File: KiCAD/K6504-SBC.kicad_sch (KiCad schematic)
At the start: 35 parts, among them J5 Barrel_Jack_Switch, SW1 RESET SW, SW2 POWER_SW, U1 R6504P, U3 74LS00, U4 74LS145, U5 R6532, U6 HM62256BLP, U7 27C256, X1 1MHz

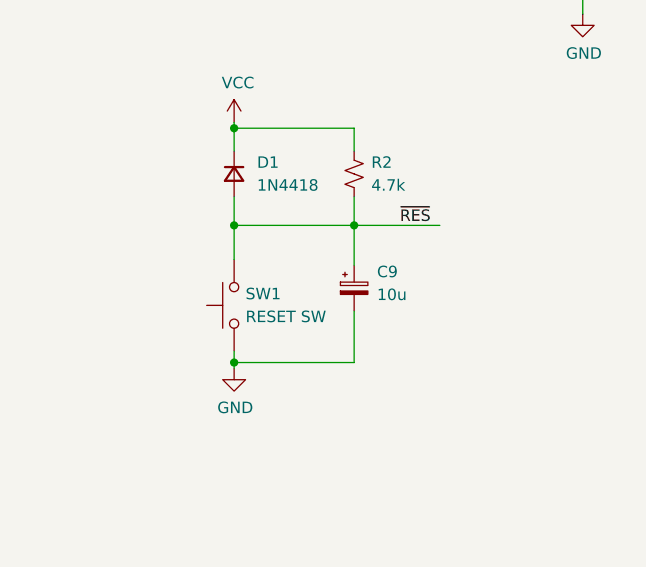
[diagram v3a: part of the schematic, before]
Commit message: 部品との関連付け追加
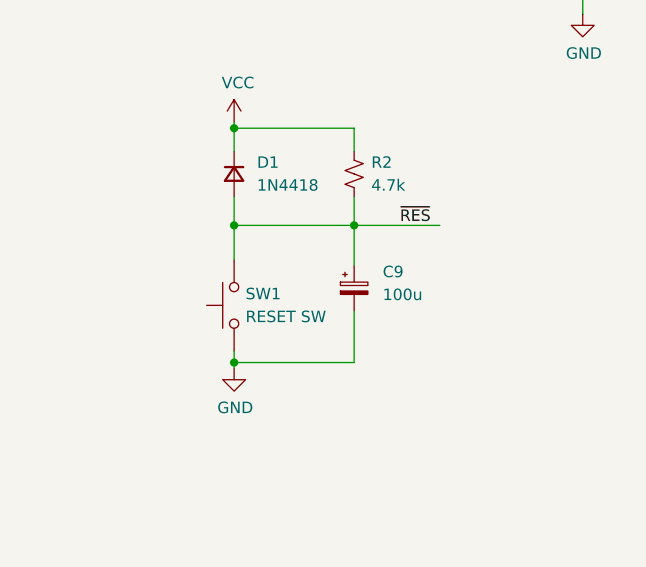
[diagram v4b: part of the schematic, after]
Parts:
- C10: footprint (none) -> Capacitor_THT:CP_Radial_D5.0mm_P2.50mm
- C9: value 10u -> 100u; footprint (none) -> Capacitor_THT:CP_Radial_D8.0mm_P2.50mm
- D1: footprint (none) -> Diode_THT:D_DO-34_SOD68_P10.16mm_Horizontal
- D2: footprint (none) -> LED_THT:LED_D3.0mm
- J5: footprint (none) -> Connector_BarrelJack:BarrelJack_Horizontal
- R2, R3: footprint (none) -> Resistor_THT:R_Axial_DIN0207_L6.3mm_D2.5mm_P10.16mm_Horizontal
- SW1: footprint (none) -> Button_Switch_THT:SW_PUSH_6mm_H4.3mm
- SW2: footprint (none) -> Connector_PinHeader_2.54mm:PinHeader_1x03_P2.54mm_Vertical
- U1, U6, U7: footprint Package_DIP:DIP-28_W15.24mm -> Package_DIP:DIP-28_W15.24mm_Socket
- U3: footprint (none) -> Package_DIP:DIP-14_W7.62mm_Socket
- U4: footprint (none) -> Package_DIP:DIP-16_W7.62mm_Socket
- U5: footprint Package_DIP:DIP-40_W15.24mm -> Package_DIP:DIP-40_W15.24mm_Socket
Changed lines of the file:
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@@
       (effects (font (size 1.27 1.27)))
     )
-    (property "Footprint" "" (at 285.115 56.896 0)
+    (property "Footprint" "Connector_BarrelJack:BarrelJack_Horizontal" (at 285.115 56.896 0)
       (effects (font (size 1.27 1.27)) hide)
     )
@@
       (effects (font (size 1.27 1.27)) (justify left))
     )
-    (property "Footprint" "Package_DIP:DIP-28_W15.24mm" (at 273.685 184.15 0)
+    (property "Footprint" "Package_DIP:DIP-28_W15.24mm_Socket" (at 273.685 184.15 0)
       (effects (font (size 1.27 1.27)) hide)
     )
@@
   (symbol (lib_id "Device:C_Polarized_Small") (at 309.245 99.06 0) (unit 1)
     (in_bom yes) (on_board yes) (dnp no) (fields_autoplaced)
-    (property "Reference" "C9" (at 311.785 97.2439 0)
-      (effects (font (size 1.27 1.27)) (justify left))
-    )
-    (property "Value" "10u" (at 311.785 99.7839 0)
-      (effects (font (size 1.27 1.27)) (justify left))
-    )
-    (property "Footprint" "" (at 309.245 99.06 0)
+    (property "Reference" "C9" (at 312.42 97.2439 0)
+      (effects (font (size 1.27 1.27)) (justify left))
+    )
+    (property "Value" "100u" (at 312.42 99.7839 0)
+      (effects (font (size 1.27 1.27)) (justify left))
+    )
+    (property "Footprint" "Capacitor_THT:CP_Radial_D8.0mm_P2.50mm" (at 309.245 99.06 0)
       (effects (font (size 1.27 1.27)) hide)
     )
@@
       (effects (font (size 1.27 1.27)) (justify left))
     )
-    (property "Footprint" "" (at 227.965 254 0)
+    (property "Footprint" "Package_DIP:DIP-14_W7.62mm_Socket" (at 227.965 254 0)
       (effects (font (size 1.27 1.27)) hide)
     )
@@
       (effects (font (size 1.27 1.27)) (justify left))
     )
-    (property "Footprint" "" (at 313.055 53.975 0)
+    (property "Footprint" "Capacitor_THT:CP_Radial_D5.0mm_P2.50mm" (at 313.055 53.975 0)
       (effects (font (size 1.27 1.27)) hide)
     )
@@
       (effects (font (size 1.27 1.27)) (justify left))
     )
-    (property "Footprint" "Package_DIP:DIP-28_W15.24mm" (at 224.79 180.34 0)
+    (property "Footprint" "Package_DIP:DIP-28_W15.24mm_Socket" (at 224.79 180.34 0)
       (effects (font (size 1.27 1.27)) hide)
     )
@@
       (effects (font (size 1.27 1.27)) (justify left))
     )
-    (property "Footprint" "" (at 324.485 50.8 0)
+    (property "Footprint" "Resistor_THT:R_Axial_DIN0207_L6.3mm_D2.5mm_P10.16mm_Horizontal" (at 324.485 50.8 0)
       (effects (font (size 1.27 1.27)) hide)
     )
@@
       (effects (font (size 1.27 1.27)))
     )
-    (property "Footprint" "" (at 302.895 46.355 0)
+    (property "Footprint" "Connector_PinHeader_2.54mm:PinHeader_1x03_P2.54mm_Vertical" (at 302.895 46.355 0)
       (effects (font (size 1.27 1.27)) hide)
     )
@@
       (effects (font (size 1.27 1.27)) (justify left))
     )
-    (property "Footprint" "Package_DIP:DIP-40_W15.24mm" (at 158.75 220.98 0)
+    (property "Footprint" "Package_DIP:DIP-40_W15.24mm_Socket" (at 158.75 220.98 0)
       (effects (font (size 1.27 1.27)) (justify left) hide)
     )
@@
       (effects (font (size 1.27 1.27)))
     )
-    (property "Footprint" "" (at 120.015 199.39 0)
+    (property "Footprint" "Package_DIP:DIP-14_W7.62mm_Socket" (at 120.015 199.39 0)
       (effects (font (size 1.27 1.27)) hide)
     )
@@
       (effects (font (size 1.27 1.27)) (justify left))
     )
-    (property "Footprint" "" (at 295.91 86.36 90)
+    (property "Footprint" "Diode_THT:D_DO-34_SOD68_P10.16mm_Horizontal" (at 295.91 86.36 90)
       (effects (font (size 1.27 1.27)) hide)
     )
@@
       (effects (font (size 1.27 1.27)))
     )
-    (property "Footprint" "" (at 229.87 104.775 0)
+    (property "Footprint" "Package_DIP:DIP-14_W7.62mm_Socket" (at 229.87 104.775 0)
       (effects (font (size 1.27 1.27)) hide)
     )
@@
       (effects (font (size 1.27 1.27)) (justify left))
     )
-    (property "Footprint" "" (at 153.035 48.895 0)
+    (property "Footprint" "Package_DIP:DIP-16_W7.62mm_Socket" (at 153.035 48.895 0)
       (effects (font (size 1.27 1.27)) hide)
     )
@@
       (effects (font (size 1.27 1.27)))
     )
-    (property "Footprint" "" (at 189.865 102.235 0)
+    (property "Footprint" "Package_DIP:DIP-14_W7.62mm_Socket" (at 189.865 102.235 0)
       (effects (font (size 1.27 1.27)) hide)
     )
@@
       (effects (font (size 1.27 1.27)))
     )
-    (property "Footprint" "" (at 229.235 122.555 0)
+    (property "Footprint" "Package_DIP:DIP-14_W7.62mm_Socket" (at 229.235 122.555 0)
       (effects (font (size 1.27 1.27)) hide)
     )
@@
       (effects (font (size 1.27 1.27)) (justify left))
     )
-    (property "Footprint" "" (at 309.245 86.36 0)
+    (property "Footprint" "Resistor_THT:R_Axial_DIN0207_L6.3mm_D2.5mm_P10.16mm_Horizontal" (at 309.245 86.36 0)
       (effects (font (size 1.27 1.27)) hide)
     )
@@
       (effects (font (size 1.27 1.27)) (justify right))
     )
-    (property "Footprint" "" (at 290.83 100.965 0)
+    (property "Footprint" "Button_Switch_THT:SW_PUSH_6mm_H4.3mm" (at 290.83 100.965 0)
       (effects (font (size 1.27 1.27)) hide)
     )
@@
       (effects (font (size 1.27 1.27)) (justify left))
     )
-    (property "Footprint" "Package_DIP:DIP-28_W15.24mm" (at 61.595 193.04 0)
+    (property "Footprint" "Package_DIP:DIP-28_W15.24mm_Socket" (at 61.595 193.04 0)
       (effects (font (size 1.27 1.27)) hide)
     )
@@
       (effects (font (size 1.27 1.27)) (justify right))
     )
-    (property "Footprint" "" (at 324.485 58.42 90)
-      (effects (font (size 1.27 1.27)) hide)
-    )
+    (property "Footprint" "LED_THT:LED_D3.0mm" (at 324.485 58.42 90)
+      (effects (font (size 1.27 1.27)) hide)
+    )

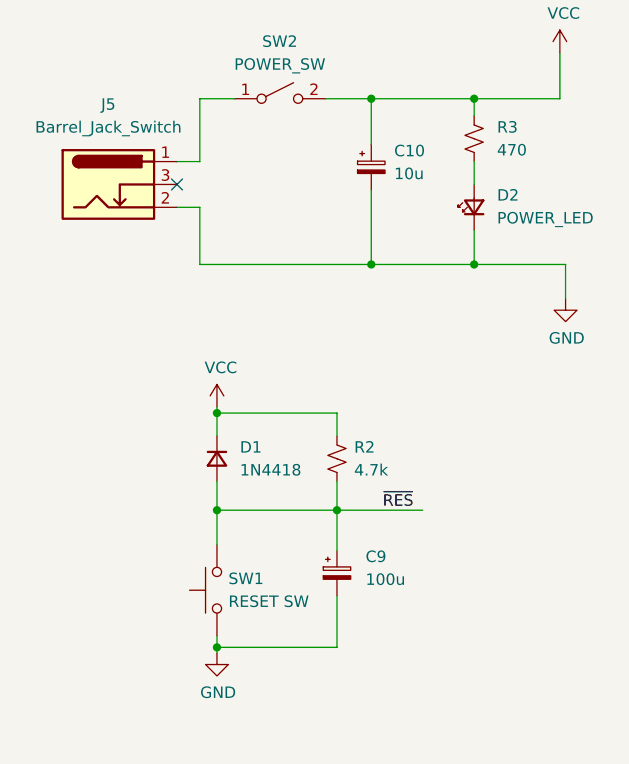
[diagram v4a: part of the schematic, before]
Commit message: コンデンサ定数修正、回路図イメージ更新
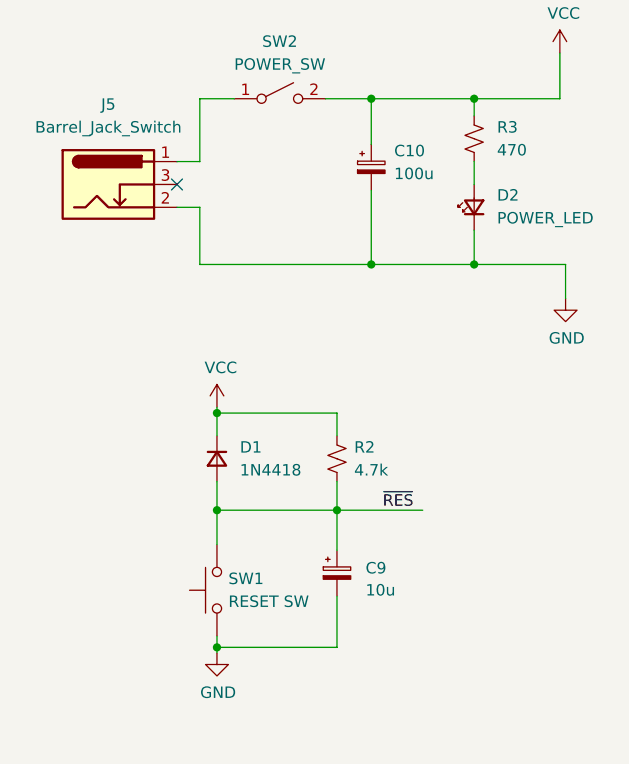
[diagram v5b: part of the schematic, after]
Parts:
- C10: value 10u -> 100u; footprint Capacitor_THT:CP_Radial_D5.0mm_P2.50mm -> Capacitor_THT:CP_Radial_D8.0mm_P2.50mm
- C9: value 100u -> 10u; footprint Capacitor_THT:CP_Radial_D8.0mm_P2.50mm -> Capacitor_THT:CP_Radial_D5.0mm_P2.50mm
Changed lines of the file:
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@@
   )
   (symbol (lib_id "Device:C_Polarized_Small") (at 309.245 99.06 0) (unit 1)
-    (in_bom yes) (on_board yes) (dnp no) (fields_autoplaced)
-    (property "Reference" "C9" (at 312.42 97.2439 0)
-      (effects (font (size 1.27 1.27)) (justify left))
-    )
-    (property "Value" "100u" (at 312.42 99.7839 0)
-      (effects (font (size 1.27 1.27)) (justify left))
-    )
-    (property "Footprint" "Capacitor_THT:CP_Radial_D8.0mm_P2.50mm" (at 309.245 99.06 0)
+    (in_bom yes) (on_board yes) (dnp no)
+    (property "Reference" "C9" (at 312.42 98.5139 0)
+      (effects (font (size 1.27 1.27)) (justify left))
+    )
+    (property "Value" "10u" (at 312.42 100.965 0)
+      (effects (font (size 1.27 1.27)) (justify left))
+    )
+    (property "Footprint" "Capacitor_THT:CP_Radial_D5.0mm_P2.50mm" (at 309.245 99.06 0)
       (effects (font (size 1.27 1.27)) hide)
     )
@@
       (effects (font (size 1.27 1.27)) (justify left))
     )
-    (property "Value" "10u" (at 315.595 54.6989 0)
-      (effects (font (size 1.27 1.27)) (justify left))
-    )
-    (property "Footprint" "Capacitor_THT:CP_Radial_D5.0mm_P2.50mm" (at 313.055 53.975 0)
-      (effects (font (size 1.27 1.27)) hide)
-    )
+    (property "Value" "100u" (at 315.595 54.6989 0)
+      (effects (font (size 1.27 1.27)) (justify left))
+    )
+    (property "Footprint" "Capacitor_THT:CP_Radial_D8.0mm_P2.50mm" (at 313.055 53.975 0)
+      (effects (font (size 1.27 1.27)) hide)
+    )

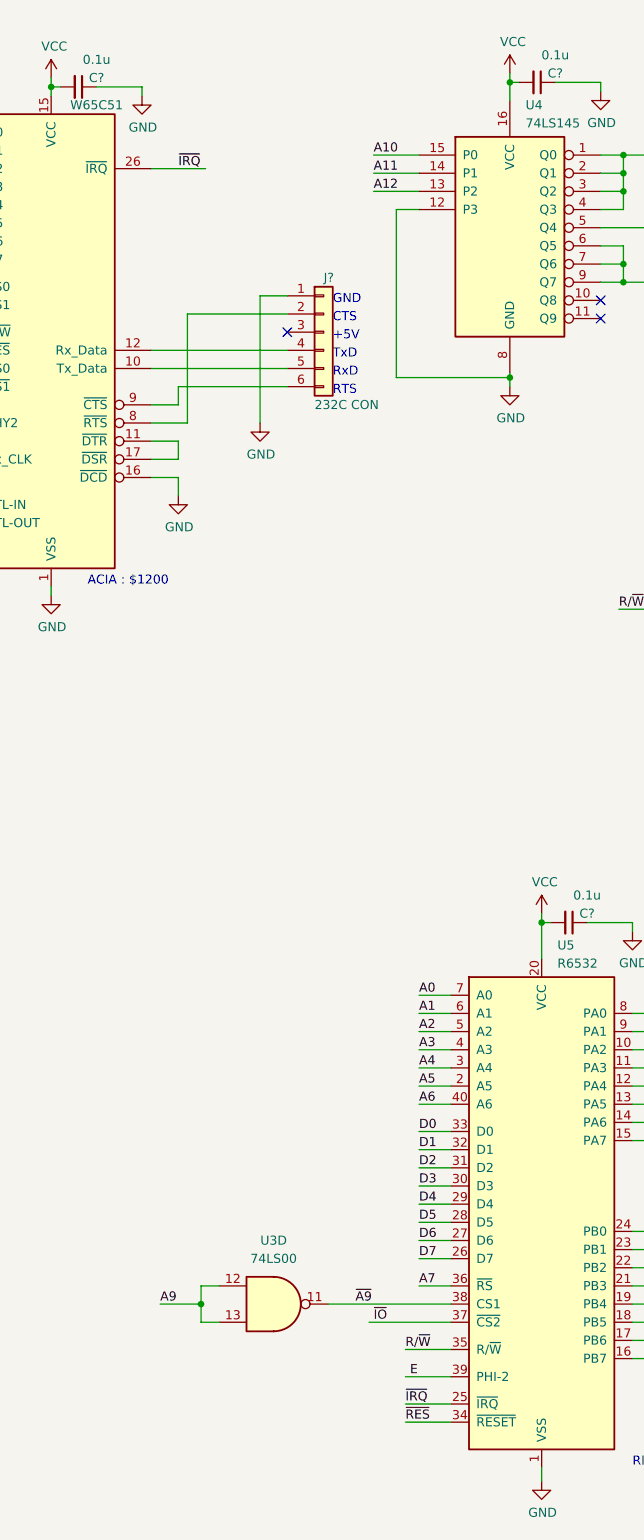
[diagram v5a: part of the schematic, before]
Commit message: 基板サイズ見直し、ガーバーデータ再出力
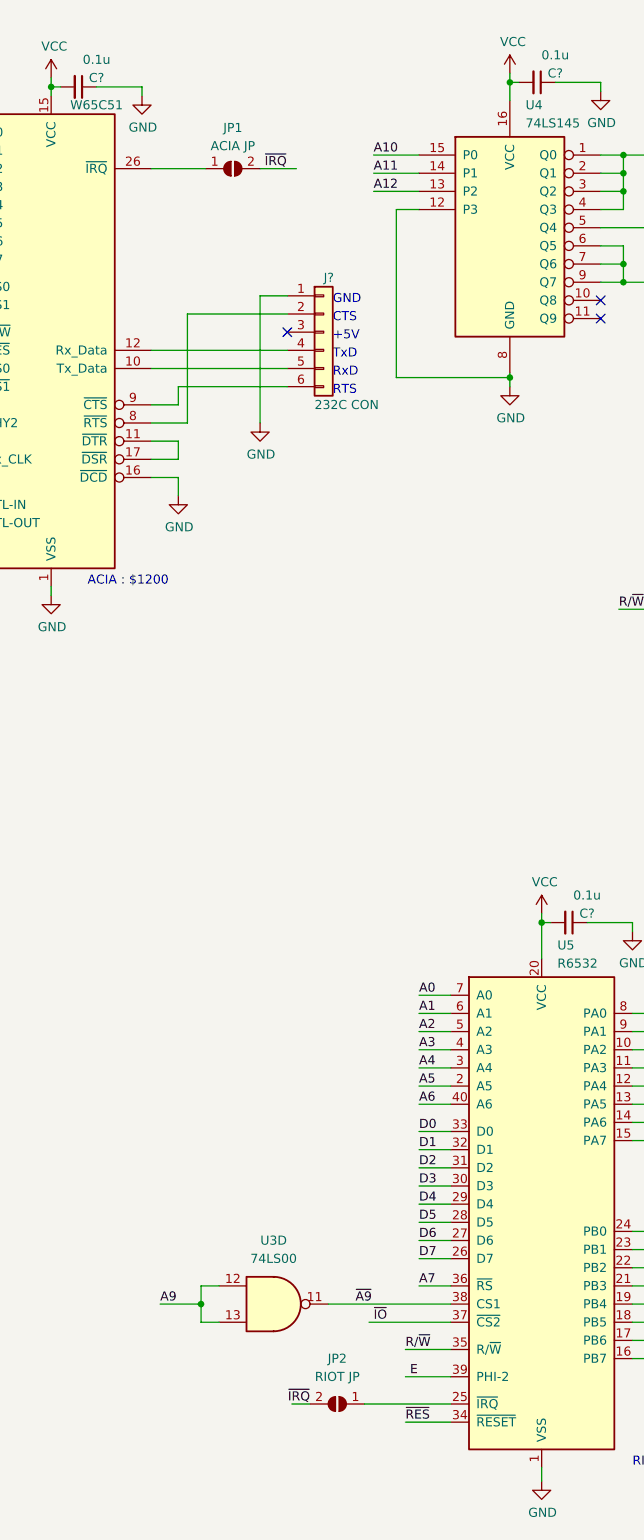
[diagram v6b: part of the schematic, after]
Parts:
- added JP1: ACIA JP, Jumper:SolderJumper-2_P1.3mm_Open_RoundedPad1.0x1.5mm, symbol Jumper:SolderJumper_2_Open
- added JP2: RIOT JP, Jumper:SolderJumper-2_P1.3mm_Open_RoundedPad1.0x1.5mm, symbol Jumper:SolderJumper_2_Open
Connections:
- net ~{IRQ}: now also JP1.2 (B), JP2.2 (B); no longer U5.25 (~{IRQ}), U?.26 (~{IRQ})
- new net: JP2.1 (A), U5.25 (~{IRQ})
- new net: JP1.1 (A), U?.26 (~{IRQ})
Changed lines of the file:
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@@
   (title_block
     (title "R6504P CPU用シングルボード・コンピューター")
-    (date "2023-07-16")
+    (date "2024-02-24")
     (rev "1")
     (company "KUNI-NET")
@@
     (stroke (width 0) (type default))
   )
-  (wire (pts (xy 138.43 213.36) (xy 144.78 213.36))
+  (wire (pts (xy 132.715 213.36) (xy 144.78 213.36))
     (stroke (width 0) (type default))
   )
@@
     (stroke (width 0) (type default))
   )
+  (wire (pts (xy 125.095 213.36) (xy 122.555 213.36))
+    (stroke (width 0) (type default))
+  )
   (wire (pts (xy 176.53 99.695) (xy 176.53 102.235))
     (stroke (width 0) (type default))
@@
     (stroke (width 0) (type default))
   )
+  (wire (pts (xy 118.11 40.64) (xy 123.19 40.64))
+    (stroke (width 0) (type default))
+  )
   (wire (pts (xy 207.645 165.1) (xy 212.09 165.1))
     (stroke (width 0) (type default))
@@
     (effects (font (size 1.27 1.27)) (justify left bottom))
   )
+  (label "~{IRQ}" (at 125.095 213.36 180) (fields_autoplaced)
+    (effects (font (size 1.27 1.27)) (justify right bottom))
+  )
   (label "A1" (at 25.4 154.94 0) (fields_autoplaced)
     (effects (font (size 1.27 1.27)) (justify left bottom))
@@
     (effects (font (size 1.27 1.27)) (justify right bottom))
   )
-  (label "~{IRQ}" (at 138.43 213.36 0) (fields_autoplaced)
-    (effects (font (size 1.27 1.27)) (justify left bottom))
-  )
   (label "PA7" (at 176.53 176.53 180) (fields_autoplaced)
     (effects (font (size 1.27 1.27)) (justify right bottom))
@@
     (effects (font (size 1.27 1.27)) (justify left bottom))
   )
-  (label "~{IRQ}" (at 106.68 40.64 0) (fields_autoplaced)
+  (label "~{IRQ}" (at 118.745 40.64 0) (fields_autoplaced)
     (effects (font (size 1.27 1.27)) (justify left bottom))
   )
@@
     )
   )
+  (symbol (lib_id "Jumper:SolderJumper_2_Open") (at 128.905 213.36 180) (unit 1)
+    (in_bom yes) (on_board yes) (dnp no) (fields_autoplaced)
+    (property "Reference" "JP2" (at 128.905 207.01 0)
+      (effects (font (size 1.27 1.27)))
+    )
+    (property "Value" "RIOT JP" (at 128.905 209.55 0)
+      (effects (font (size 1.27 1.27)))
+    )
+    (property "Footprint" "Jumper:SolderJumper-2_P1.3mm_Open_RoundedPad1.0x1.5mm" (at 128.905 213.36 0)
+      (effects (font (size 1.27 1.27)) hide)
+    )
+    (property "Datasheet" "~" (at 128.905 213.36 0)
+      (effects (font (size 1.27 1.27)) hide)
+    )
+    (pin "1")
+    (pin "2")
+    (instances
+      (project "K6504-SBC"
+        (path "/e35d21eb-7dcd-43f6-9b26-32dbfb5b8b9d"
+          (reference "JP2") (unit 1)
+        )
+      )
+    )
+  )
   (symbol (lib_id "power:GND") (at 227.965 268.605 0) (unit 1)
     (in_bom yes) (on_board yes) (dnp no)
@@
         )
       )
+    )
+  )
+  (symbol (lib_id "Jumper:SolderJumper_2_Open") (at 114.3 40.64 0) (unit 1)
+    (in_bom yes) (on_board yes) (dnp no) (fields_autoplaced)
+    (property "Reference" "JP1" (at 114.3 34.925 0)
+      (effects (font (size 1.27 1.27)))
+    )
+    (property "Value" "ACIA JP" (at 114.3 37.465 0)
+      (effects (font (size 1.27 1.27)))
+    )
+    (property "Footprint" "Jumper:SolderJumper-2_P1.3mm_Open_RoundedPad1.0x1.5mm" (at 114.3 40.64 0)
+      (effects (font (size 1.27 1.27)) hide)
+    )
+    (property "Datasheet" "~" (at 114.3 40.64 0)
+      (effects (font (size 1.27 1.27)) hide)
+    )
+    (pin "1")
+    (pin "2")
+    (instances
+      (project "K6504-SBC"
+        (path "/e35d21eb-7dcd-43f6-9b26-32dbfb5b8b9d"
+          (reference "JP1") (unit 1)
+        )
+      )
